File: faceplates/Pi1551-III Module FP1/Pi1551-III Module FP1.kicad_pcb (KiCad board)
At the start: 2 copper layers, 100 x 35 mm, 9 parts, among them M1 Mounting_Pin, M2 Mounting_Pin, M3 Mounting_Pin, M4 Mounting_Pin

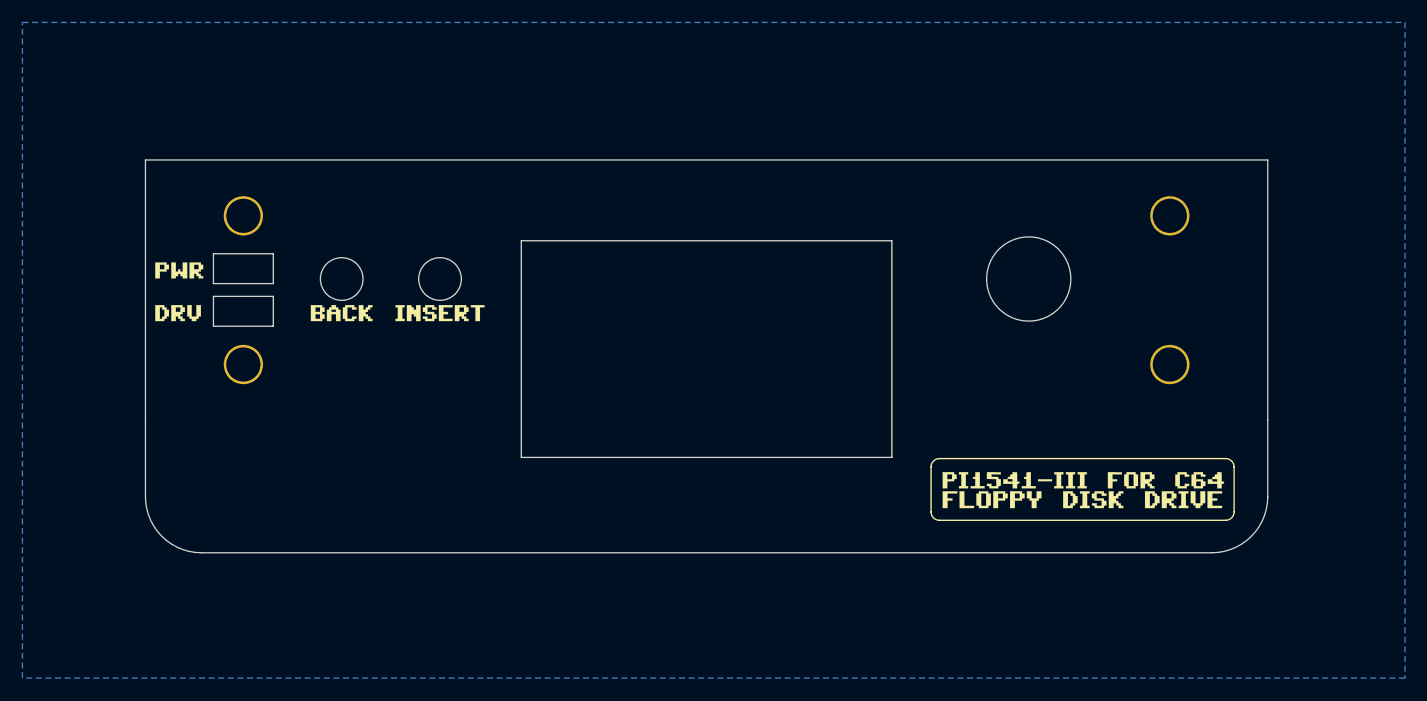
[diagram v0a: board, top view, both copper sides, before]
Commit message: PI1551 branding and Microgramma font labels
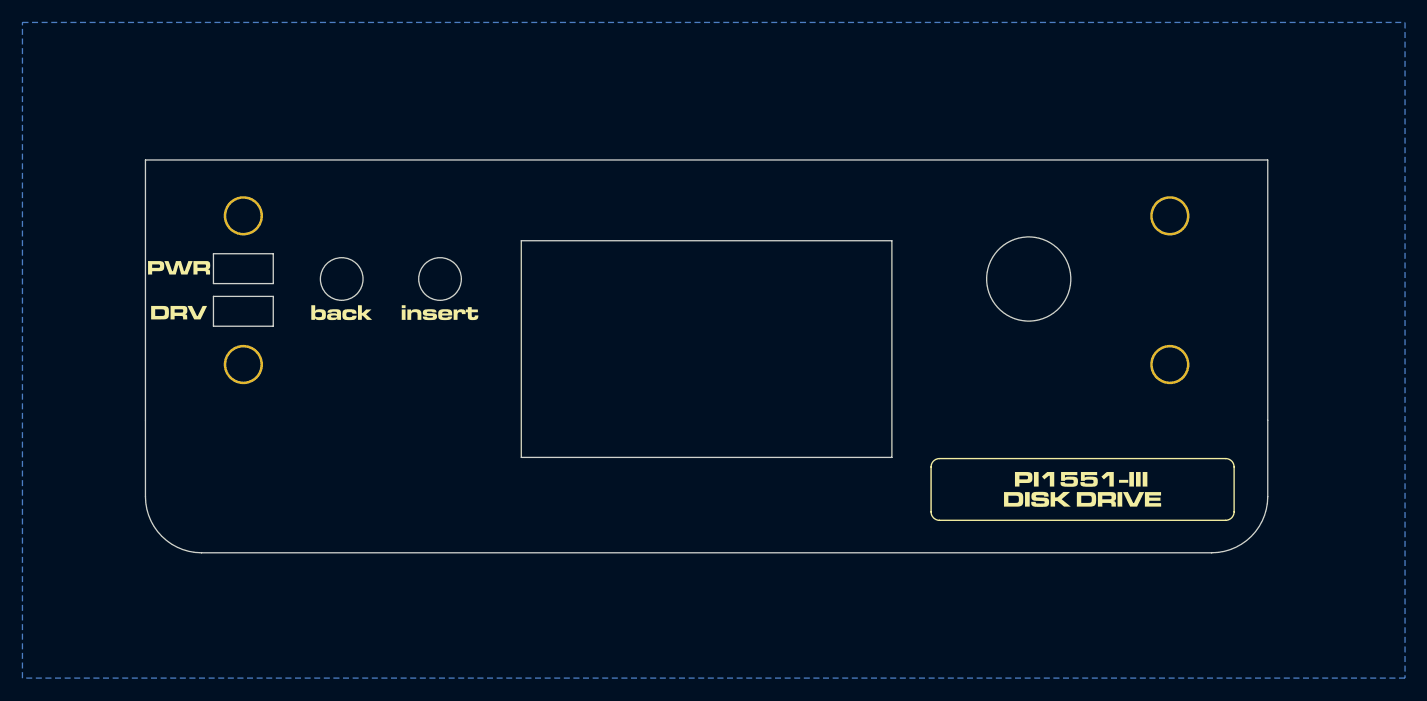
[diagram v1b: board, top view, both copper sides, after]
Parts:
- removed G***: LOGO, Pi1541:Pi1541-PWR
- removed G***: LOGO, Pi1541:Pi1541-DRV
- removed G***: LOGO, Pi1541:Pi1541-Insert
- removed G***: LOGO, Pi1541:Pi1541-Back
- removed G***: LOGO, Pi1541:Pi1541-Decal
- added kibuzzard-69865524: G***, kibuzzard-69865524, F.Cu at (174.6, 140.3)
- added kibuzzard-6986556E: G***, kibuzzard-6986556E, F.Cu at (117.3, 124.6)
- added kibuzzard-69865582: G***, kibuzzard-69865582, F.Cu at (108.6, 124.6)
- added kibuzzard-6986560D: G***, kibuzzard-6986560D, F.Cu at (94.1, 120.6)
- added kibuzzard-69865656: G***, kibuzzard-69865656, F.Cu at (94.1, 124.6)
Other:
- board text added: "JLCJLCJLCJLC"
